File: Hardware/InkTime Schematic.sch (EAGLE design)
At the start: 105 parts, among them IC1 BQ25180YBGR, IC2 DRV2605YZFR, IC3 BMA421, IC9 RT6160AWSC, J1 503480-2400, J2 TC2030-IDC, J4 KH-TYPE-C-16P, Q2 20V/4.2A/52mΩ/1.4W, Q3 SI1308EDL-T1-GE3, U1 NRF52840_QF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

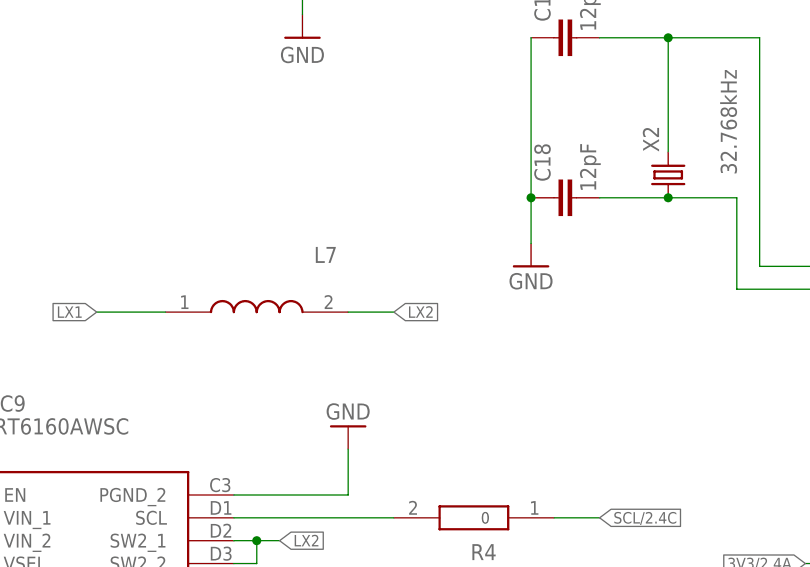
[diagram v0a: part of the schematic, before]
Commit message: Add missing reference Fixes #1
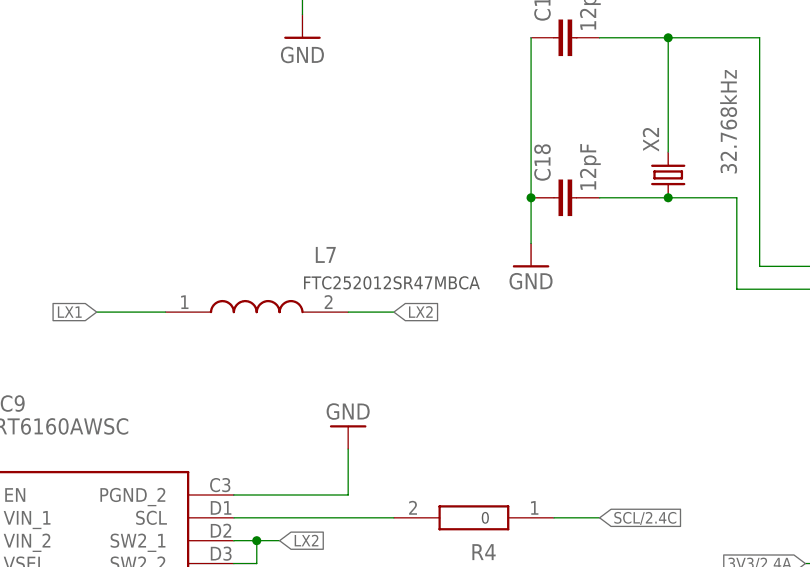
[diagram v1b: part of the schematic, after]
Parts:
- L7: value MLP2016SR47MT0S1_FTC252012SR47MBCA -> FTC252012SR47MBCA
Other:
- note added: "FTC252012SR47MBCA"

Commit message: Fix nets and symbol naming inconsistencies
Fixes #8
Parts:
- X2: value 32.768kHz -> 32.768KHz; device adafruit:CRYSTALHC49S -> InkTime_v5:NORDIC_NRF_1_XTAL_32KHZ
- renumbered D1 to D3
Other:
- note added: "P0.00/XL1"
- note added: "P0.01/XL2"
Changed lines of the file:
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@@
 <part name="C5" library="InkTime_v5" library_urn="urn:adsk.wipprod:fs.file:vf.UGCviqsKRuyr22hNdtfhcA" deviceset="NORDIC_NRF_3_CAPACITOR" device="_0201_L" value="100nF"/>
 <part name="SUPPLY12" library="InkTime_v5" library_urn="urn:adsk.wipprod:fs.file:vf.UGCviqsKRuyr22hNdtfhcA" deviceset="POWER_SYMBOLS_GND-BAR" device="" value="GND"/>
-<part name="X2" library="adafruit" library_urn="urn:adsk.eagle:library:420" deviceset="CRYSTAL" device="HC49S" package3d_urn="urn:adsk.eagle:package:6240901/1" value="32.768kHz"/>
 <part name="C17" library="InkTime_v5" library_urn="urn:adsk.wipprod:fs.file:vf.UGCviqsKRuyr22hNdtfhcA" deviceset="NORDIC_NRF_3_CAPACITOR" device="_0201_L" value="12pF"/>
 <part name="C18" library="InkTime_v5" library_urn="urn:adsk.wipprod:fs.file:vf.UGCviqsKRuyr22hNdtfhcA" deviceset="NORDIC_NRF_3_CAPACITOR" device="_0201_L" value="12pF"/>
@@
 <part uuid="0xABCDEF1D" name="Q2" library="Libraria_DANI" library_urn="urn:adsk.wipprod:fs.file:vf.6thThEW2Taar68j57l-5Ng" deviceset="ESP32_C6_LIBRARY_4_ESP32_WROVER_SPARKFUN-DISCRETESEMI_MOSFET_PCH" device="-DMG2305UX-7" value="20V/4.2A/52mΩ/1.4W"/>
 <part name="R_PWR_EPD1" library="Libraria_DANI" library_urn="urn:adsk.wipprod:fs.file:vf.6thThEW2Taar68j57l-5Ng" deviceset="CPF0201D7K68C1_CPF0201D7K68C1" device="" value="10K"/>
-<part uuid="0xABCDEF19" name="D1" library="InkTime_v5" library_urn="urn:adsk.wipprod:fs.file:vf.UGCviqsKRuyr22hNdtfhcA" deviceset="ESP32_C6_LIBRARY_3_USBLC6-2SC6Y" device="" value="USBLC6-2SC6Y"/>
+<part uuid="0xABCDEF19" name="D3" library="InkTime_v5" library_urn="urn:adsk.wipprod:fs.file:vf.UGCviqsKRuyr22hNdtfhcA" deviceset="ESP32_C6_LIBRARY_3_USBLC6-2SC6Y" device="" value="USBLC6-2SC6Y"/>
 <part uuid="0xABCDEF0B" name="IC2" library="InkTime_v5" library_urn="urn:adsk.wipprod:fs.file:vf.JsBoF3kMSYaj81cftw4Bpw" deviceset="DRV2605YZFR_DRV2605YZFR" device="" value="DRV2605YZFR"/>
 <part name="SUPPLY55" library="Tutorial - Fusion 360" library_urn="urn:adsk.eagle:library:16997205" deviceset="GND-BAR" device="" value="GND"/>
@@
 <part name="SUPPLY60" library="InkTime_v5" library_urn="urn:adsk.wipprod:fs.file:vf.UGCviqsKRuyr22hNdtfhcA" deviceset="TUTORIAL---FUSION-360_GND-BAR" device="" value="GND"/>
 <part name="SUPPLY61" library="InkTime_v5" library_urn="urn:adsk.wipprod:fs.file:vf.UGCviqsKRuyr22hNdtfhcA" deviceset="TUTORIAL---FUSION-360_GND-BAR" device="" value="GND"/>
+<part name="X2" library="InkTime_v5" library_urn="urn:adsk.wipprod:fs.file:vf.UGCviqsKRuyr22hNdtfhcA" deviceset="NORDIC_NRF_1_XTAL_32KHZ" device="" value="32.768KHz"/>
 </parts>
 <sheets>
@@
 <text x="154.94" y="-251.46" size="1.27" layer="97" rot="R90" align="center-right">10k</text>
 <text x="-55.88" y="66.04" size="1.4224" layer="97">FTC252012SR47MBCA</text>
+<text x="17.78" y="68.58" size="1.778" layer="97">P0.00/XL1</text>
+<text x="17.78" y="66.04" size="1.778" layer="97">P0.01/XL2</text>
 </plain>
 <instances>
@@
 <attribute name="VALUE" x="7.62" y="74.295" size="1.778" layer="96" align="center"/>
 </instance>
-<instance part="X2" gate="G$1" x="-15.24" y="78.74" smashed="yes" rot="R90">
-<attribute name="NAME" x="-16.256" y="81.28" size="1.778" layer="95" rot="R90"/>
-<attribute name="VALUE" x="-7.62" y="78.74" size="1.778" layer="96" rot="R90"/>
-</instance>
 <instance part="C17" gate="C$1" x="-25.4" y="93.98" smashed="yes" rot="R270">
 <attribute name="NAME" x="-30.099" y="100.076" size="1.778" layer="95" rot="R270"/>
@@
 <attribute name="NAME" x="1.27" y="-191.77" size="1.778" layer="95" rot="R90" align="center-left"/>
 </instance>
-<instance part="D1" gate="G$1" x="162.56" y="-342.9" smashed="yes">
+<instance part="D3" gate="G$1" x="162.56" y="-342.9" smashed="yes">
 <attribute name="NAME" x="191.77" y="-335.28" size="1.778" layer="95" align="center-left"/>
 <attribute name="VALUE" x="191.77" y="-337.82" size="1.778" layer="96" align="center-left"/>
@@
 <instance part="SUPPLY61" gate="G$1" x="152.4" y="-307.34" smashed="yes">
 <attribute name="VALUE" x="152.4" y="-309.88" size="1.778" layer="96" align="bottom-center"/>
+</instance>
+<instance part="X2" gate="X$1" x="-12.7" y="78.74" smashed="yes" rot="R90">
+<attribute name="NAME" x="-16.256" y="78.74" size="1.778" layer="95" rot="R90"/>
+<attribute name="VALUE" x="-8.89" y="78.74" size="1.778" layer="96" rot="R90"/>
 </instance>
 </instances>
@@
 <wire x1="160.02" y1="-345.44" x2="160.02" y2="-353.06" width="0.1524" layer="91"/>
 <pinref part="SUPPLY52" gate="G$1" pin="GND"/>
-<pinref part="D1" gate="G$1" pin="GND"/>
+<pinref part="D3" gate="G$1" pin="GND"/>
 </segment>
 <segment>
@@
 <wire x1="35.56" y1="68.58" x2="-5.08" y2="68.58" width="0.1524" layer="91"/>
 <wire x1="-5.08" y1="68.58" x2="-5.08" y2="93.98" width="0.1524" layer="91"/>
-<wire x1="-5.08" y1="93.98" x2="-15.24" y2="93.98" width="0.1524" layer="91"/>
-<wire x1="-15.24" y1="93.98" x2="-15.24" y2="81.28" width="0.1524" layer="91"/>
-<pinref part="X2" gate="G$1" pin="2"/>
-<wire x1="-15.24" y1="93.98" x2="-22.86" y2="93.98" width="0.1524" layer="91"/>
+<wire x1="-5.08" y1="93.98" x2="-12.7" y2="93.98" width="0.1524" layer="91"/>
 <pinref part="C17" gate="C$1" pin="1"/>
-<junction x="-15.24" y="93.98"/>
+<pinref part="X2" gate="X$1" pin="2"/>
+<wire x1="-12.7" y1="93.98" x2="-22.86" y2="93.98" width="0.1524" layer="91"/>
+<wire x1="-12.7" y1="83.82" x2="-12.7" y2="93.98" width="0.1524" layer="91"/>
+<junction x="-12.7" y="93.98"/>
 </segment>
 </net>
@@
 <wire x1="35.56" y1="66.04" x2="-7.62" y2="66.04" width="0.1524" layer="91"/>
 <wire x1="-7.62" y1="66.04" x2="-7.62" y2="76.2" width="0.1524" layer="91"/>
-<wire x1="-7.62" y1="76.2" x2="-15.24" y2="76.2" width="0.1524" layer="91"/>
-<pinref part="X2" gate="G$1" pin="1"/>
-<wire x1="-15.24" y1="76.2" x2="-22.86" y2="76.2" width="0.1524" layer="91"/>
+<wire x1="-7.62" y1="76.2" x2="-12.7" y2="76.2" width="0.1524" layer="91"/>
 <pinref part="C18" gate="C$1" pin="1"/>
-<junction x="-15.24" y="76.2"/>
+<pinref part="X2" gate="X$1" pin="1"/>
+<wire x1="-12.7" y1="76.2" x2="-22.86" y2="76.2" width="0.1524" layer="91"/>
+<junction x="-12.7" y="76.2"/>
 </segment>
 </net>
@@
 <wire x1="162.56" y1="-347.98" x2="157.48" y2="-347.98" width="0.1524" layer="91"/>
 <label x="157.48" y="-347.98" size="1.27" layer="95" rot="R180" xref="yes"/>
-<pinref part="D1" gate="G$1" pin="I/O2_1"/>
+<pinref part="D3" gate="G$1" pin="I/O2_1"/>
 </segment>
 </net>
@@
 <wire x1="162.56" y1="-342.9" x2="157.48" y2="-342.9" width="0.1524" layer="91"/>
 <label x="157.48" y="-342.9" size="1.27" layer="95" rot="R180" xref="yes"/>
-<pinref part="D1" gate="G$1" pin="I/O1_1"/>
+<pinref part="D3" gate="G$1" pin="I/O1_1"/>
 </segment>
 </net>
@@
 <wire x1="195.58" y1="-345.44" x2="198.12" y2="-345.44" width="0.1524" layer="91"/>
 <label x="198.12" y="-345.44" size="1.27" layer="95" xref="yes"/>
-<pinref part="D1" gate="G$1" pin="VBUS"/>
+<pinref part="D3" gate="G$1" pin="VBUS"/>
 </segment>
 <segment>
@@
 <wire x1="195.58" y1="-342.9" x2="198.12" y2="-342.9" width="0.1524" layer="91"/>
 <label x="198.12" y="-342.9" size="1.27" layer="95" xref="yes"/>
-<pinref part="D1" gate="G$1" pin="I/O1_2"/>
+<pinref part="D3" gate="G$1" pin="I/O1_2"/>
 </segment>
 </net>
@@
 <wire x1="195.58" y1="-347.98" x2="198.12" y2="-347.98" width="0.1524" layer="91"/>
 <label x="198.12" y="-347.98" size="1.27" layer="95" xref="yes"/>
-<pinref part="D1" gate="G$1" pin="I/O2_2"/>
-</segment>
-</net>
+<pinref part="D3" gate="G$1" pin="I/O2_2"/>
+</segment>
+</net>

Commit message: Update Schematic and Upload PrintOut
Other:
- note removed: "5K1"
